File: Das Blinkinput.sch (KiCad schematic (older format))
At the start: 11 parts, among them P101 CONN_01X02, P102 CONN_01X01, P103 CONN_01X01, P104 CONN_01X01, P105 CONN_01X05, U101 LP2980IM5-3.0/NOPB

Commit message: Added photodiode component to new local footprint library
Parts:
- C101, C102: footprint (none) -> Capacitors_SMD:C_0805_HandSoldering
- P101: footprint (none) -> Pin_Headers:Pin_Header_Straight_1x02
- P102, P103, P104: footprint (none) -> Pin_Headers:Pin_Header_Straight_1x01
- P105: footprint (none) -> Pin_Headers:Pin_Header_Straight_1x05
- R101, R102, R103: footprint (none) -> Resistors_SMD:R_0805_HandSoldering
- U101: footprint (none) -> Housings_SOT-23_SOT-143_TSOT-6:SOT-23-5
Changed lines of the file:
@@
 F 0 "P105" H 8250 1900 50  0000 C CNN
 F 1 "CONN_01X05" V 8350 1600 50  0000 C CNN
-F 2 "" H 8250 1600 60  0000 C CNN
+F 2 "Pin_Headers:Pin_Header_Straight_1x05" H 8250 1600 60  0001 C CNN
 F 3 "" H 8250 1600 60  0000 C CNN
 	1    8250 1600
@@
 F 0 "P101" H 750 1800 50  0000 C CNN
 F 1 "CONN_01X02" V 850 1650 50  0000 C CNN
-F 2 "" H 750 1650 60  0000 C CNN
+F 2 "Pin_Headers:Pin_Header_Straight_1x02" H 750 1650 60  0001 C CNN
 F 3 "" H 750 1650 60  0000 C CNN
 	1    750  1650
@@
 F 0 "U101" H 2900 1450 60  0000 C CNN
 F 1 "LP2980IM5-3.0/NOPB" H 2700 2350 60  0000 C CNN
-F 2 "" H 2700 1900 60  0000 C CNN
+F 2 "Housings_SOT-23_SOT-143_TSOT-6:SOT-23-5" H 2700 1900 60  0001 C CNN
 F 3 "" H 2700 1900 60  0000 C CNN
 	1    2700 1900
@@
 F 0 "C101" H 1375 2050 50  0000 L CNN
 F 1 "1U" H 1375 1850 50  0000 L CNN
-F 2 "" H 1388 1800 30  0000 C CNN
+F 2 "Capacitors_SMD:C_0805_HandSoldering" H 1388 1800 30  0001 C CNN
 F 3 "" H 1350 1950 60  0000 C CNN
 	1    1350 1950
@@
 F 0 "C102" H 3725 2150 50  0000 L CNN
 F 1 "1U" H 3725 1950 50  0000 L CNN
-F 2 "" H 3738 1900 30  0000 C CNN
+F 2 "Capacitors_SMD:C_0805_HandSoldering" H 3738 1900 30  0001 C CNN
 F 3 "" H 3700 2050 60  0000 C CNN
 	1    3700 2050
@@
 F 0 "R101" V 1730 2300 50  0000 C CNN
 F 1 "0" V 1650 2300 50  0000 C CNN
-F 2 "" V 1580 2300 30  0000 C CNN
+F 2 "Resistors_SMD:R_0805_HandSoldering" V 1580 2300 30  0001 C CNN
 F 3 "" H 1650 2300 30  0000 C CNN
 	1    1650 2300
@@
 F 0 "R102" V 2280 5150 50  0000 C CNN
 F 1 "10K" V 2200 5150 50  0000 C CNN
-F 2 "" V 2130 5150 30  0000 C CNN
+F 2 "Resistors_SMD:R_0805_HandSoldering" V 2130 5150 30  0001 C CNN
 F 3 "" H 2200 5150 30  0000 C CNN
 	1    2200 5150
@@
 F 0 "R103" V 2280 5700 50  0000 C CNN
 F 1 "10K" V 2200 5700 50  0000 C CNN
-F 2 "" V 2130 5700 30  0000 C CNN
+F 2 "Resistors_SMD:R_0805_HandSoldering" V 2130 5700 30  0001 C CNN
 F 3 "" H 2200 5700 30  0000 C CNN
 	1    2200 5700
@@
 F 0 "P103" H 3600 1150 50  0000 C CNN
 F 1 "CONN_01X01" V 3700 1050 50  0000 C CNN
-F 2 "" H 3600 1050 60  0000 C CNN
+F 2 "Pin_Headers:Pin_Header_Straight_1x01" H 3600 1050 60  0001 C CNN
 F 3 "" H 3600 1050 60  0000 C CNN
 	1    3600 1050
@@
 F 0 "P102" H 2700 4950 50  0000 C CNN
 F 1 "CONN_01X01" V 2800 4850 50  0000 C CNN
-F 2 "" H 2700 4850 60  0000 C CNN
+F 2 "Pin_Headers:Pin_Header_Straight_1x01" H 2700 4850 60  0001 C CNN
 F 3 "" H 2700 4850 60  0000 C CNN
 	1    2700 4850
@@
 F 0 "P104" H 3650 3250 50  0000 C CNN
 F 1 "CONN_01X01" V 3750 3150 50  0000 C CNN
-F 2 "" H 3650 3150 60  0000 C CNN
+F 2 "Pin_Headers:Pin_Header_Straight_1x01" H 3650 3150 60  0001 C CNN
 F 3 "" H 3650 3150 60  0000 C CNN
 	1    3650 3150

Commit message: Routed remainder of lines and added test points with lables
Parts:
- added P106: CONN_01X01, Pin_Headers:Pin_Header_Straight_1x01, symbol CONN_01X01
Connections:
- net Channel1Photodetect/REF_OUT: now also P106.1 (P1)
- net Channel1Photodetect/Channel1_Out renamed Channel1Photodetect/PD2
- net Channel2Photodetect/Channel2_Out renamed Channel2Photodetect/PD3
- net Channel3Photodetect/Channel3_Out renamed Channel3Photodetect/PD5
- net Channel4Photodetect/Channel4_Out renamed Channel4Photodetect/PD4
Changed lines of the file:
@@
 F0 "Channel1Photodetect" 60
 F1 "Channel1Photodetect.sch" 60
-F2 "Channel1_Out" I R 6500 1400 60
-F3 "REF_OUT" I L 5050 1700 60
+F2 "REF_OUT" I L 5050 1700 60
+F3 "PD2" I R 6500 1400 60
 $EndSheet
 $Sheet
@@
 F0 "Channel2Photodetect" 60
 F1 "Channel2Photodetect.sch" 60
-F2 "Channel2_Out" I R 6500 2950 60
-F3 "REF_IN" I L 5100 3300 60
+F2 "REF_IN" I L 5100 3300 60
+F3 "PD3" I R 6500 2950 60
 $EndSheet
 $Sheet
@@
 F0 "Channel4Photodetect" 60
 F1 "Channel4Photodetect.sch" 60
-F2 "Channel4_Out" I R 6500 5900 60
-F3 "REF_IN" I L 5100 6200 60
+F2 "REF_IN" I L 5100 6200 60
+F3 "PD4" I R 6500 5900 60
 $EndSheet
 $Sheet
@@
 F0 "Channel3Photodetect" 60
 F1 "Channel3Photodetect.sch" 60
-F2 "Channel3_Out" I R 6600 4400 60
-F3 "REF_IN" I L 5150 4750 60
+F2 "REF_IN" I L 5150 4750 60
+F3 "PD5" I R 6600 4400 60
 $EndSheet
 $Comp
@@
 	1    0    0    -1
 $EndComp
-Wire Wire Line
-	5050 1700 4850 1700
-Wire Wire Line
-	4850 1700 4850 6200
-Wire Wire Line
-	4850 3300 5100 3300
-Wire Wire Line
-	4850 4750 5150 4750
-Connection ~ 4850 3300
-Wire Wire Line
-	4850 6200 5100 6200
-Connection ~ 4850 4750
-Wire Wire Line
-	8050 1400 6500 1400
-Wire Wire Line
-	6500 2950 6800 2950
-Wire Wire Line
-	6800 2950 6800 1500
-Wire Wire Line
-	6800 1500 8050 1500
-Wire Wire Line
-	6600 4400 7000 4400
-Wire Wire Line
-	7000 4400 7000 1600
-Wire Wire Line
-	7000 1600 8050 1600
-Wire Wire Line
-	6500 5900 7200 5900
-Wire Wire Line
-	7200 5900 7200 1700
-Wire Wire Line
-	7200 1700 8050 1700
-Wire Wire Line
-	8050 1800 7850 1800
-Wire Wire Line
-	7850 1800 7850 2450
-Wire Wire Line
-	1100 1900 1100 1700
-Wire Wire Line
-	1100 1700 950  1700
-Wire Wire Line
-	950  1600 1900 1600
-Wire Wire Line
-	1350 1600 1350 1800
-Connection ~ 1350 1600
-Wire Wire Line
-	1350 2100 1350 2800
-Wire Wire Line
-	1350 2800 3700 2800
-Wire Wire Line
-	2700 2800 2700 2600
-Wire Wire Line
-	3700 2800 3700 2200
-Connection ~ 2700 2800
-Wire Wire Line
-	3500 1600 4000 1600
-Wire Wire Line
-	3700 1600 3700 1900
 $Comp
 L R R101
@@
 	1    0    0    -1
 $EndComp
-Wire Wire Line
-	1650 2150 1650 1800
-Wire Wire Line
-	1650 1800 1900 1800
-Wire Wire Line
-	1650 2450 1650 2800
-Connection ~ 1650 2800
-Connection ~ 3700 1600
 Text GLabel 4000 1600 2    60   Input ~ 0
 3V
@@
 Text GLabel 1900 4700 0    60   Input ~ 0
 3V
-Wire Wire Line
-	1900 4700 2200 4700
-Wire Wire Line
-	2200 4700 2200 5000
-Wire Wire Line
-	2200 5300 2200 5550
-Wire Wire Line
-	2200 5850 2200 6300
 $Comp
 L GND #PWR03
@@
 	1    0    0    -1
 $EndComp
-Wire Wire Line
-	2450 2850 2450 2800
-Connection ~ 2450 2800
 $Comp
 L GND #PWR04
@@
 	1    0    0    -1
 $EndComp
-Wire Wire Line
-	2200 5400 2850 5400
-Connection ~ 2200 5400
 Text GLabel 2850 5400 2    60   Input ~ 0
 VGND
@@
 	0    -1   -1   0
 $EndComp
-Wire Wire Line
-	3600 1250 3600 1600
-Connection ~ 3600 1600
 $Comp
 L CONN_01X01 P102
@@
 	0    -1   -1   0
 $EndComp
-Wire Wire Line
-	2700 5050 2700 5400
-Connection ~ 2700 5400
 $Comp
 L CONN_01X01 P104
@@
 	0    1    1    0
 $EndComp
+Connection ~ 3650 2800
 Wire Wire Line
 	3650 2950 3650 2800
-Connection ~ 3650 2800
+Connection ~ 2700 5400
+Wire Wire Line
+	2700 5050 2700 5400
+Connection ~ 3600 1600
+Wire Wire Line
+	3600 1250 3600 1600
+Connection ~ 2200 5400
+Wire Wire Line
+	2200 5400 2850 5400
+Connection ~ 2450 2800
+Wire Wire Line
+	2450 2850 2450 2800
+Wire Wire Line
+	2200 5850 2200 6300
+Wire Wire Line
+	2200 5300 2200 5550
+Wire Wire Line
+	2200 4700 2200 5000
+Wire Wire Line
+	1900 4700 2200 4700
+Connection ~ 3700 1600
+Connection ~ 1650 2800
+Wire Wire Line
+	1650 2450 1650 2800
+Wire Wire Line
+	1650 1800 1900 1800
+Wire Wire Line
+	1650 2150 1650 1800
+Wire Wire Line
+	3700 1600 3700 1900
+Wire Wire Line
+	3500 1600 4000 1600
+Connection ~ 2700 2800
+Wire Wire Line
+	3700 2800 3700 2200
+Wire Wire Line
+	2700 2800 2700 2600
+Wire Wire Line
+	1350 2800 3700 2800
+Wire Wire Line
+	1350 2100 1350 2800
+Connection ~ 1350 1600
+Wire Wire Line
+	1350 1600 1350 1800
+Wire Wire Line
+	950  1600 1900 1600
+Wire Wire Line
+	1100 1700 950  1700
+Wire Wire Line
+	1100 1900 1100 1700
+Wire Wire Line
+	7850 1800 7850 2450
+Wire Wire Line
+	8050 1800 7850 1800
+Wire Wire Line
+	7200 1700 8050 1700
+Wire Wire Line
+	7200 5900 7200 1700
+Wire Wire Line
+	6500 5900 7200 5900
+Wire Wire Line
+	7000 1600 8050 1600
+Wire Wire Line
+	7000 4400 7000 1600
+Wire Wire Line
+	6600 4400 7000 4400
+Wire Wire Line
+	6800 1500 8050 1500
+Wire Wire Line
+	6800 2950 6800 1500
+Wire Wire Line
+	6500 2950 6800 2950
+Wire Wire Line
+	8050 1400 6500 1400
+Connection ~ 4850 4750
+Wire Wire Line
+	4850 6200 5100 6200
+Connection ~ 4850 3300
+Wire Wire Line
+	4850 4750 5150 4750
+Wire Wire Line
+	4850 3300 5100 3300
+Wire Wire Line
+	4850 1700 4850 6200
+Wire Wire Line
+	5050 1700 4850 1700
+$Comp
+L CONN_01X01 P106
+U 1 1 5560D7BE
+P 4450 4400
+F 0 "P106" H 4450 4500 50  0000 C CNN
+F 1 "CONN_01X01" V 4550 4400 50  0000 C CNN
+F 2 "Pin_Headers:Pin_Header_Straight_1x01" H 4450 4400 60  0001 C CNN
+F 3 "" H 4450 4400 60  0000 C CNN
+	1    4450 4400
+	-1   0    0    1
+$EndComp
+Wire Wire Line
+	4650 4400 4850 4400
+Connection ~ 4850 4400
 $EndSCHEMATC

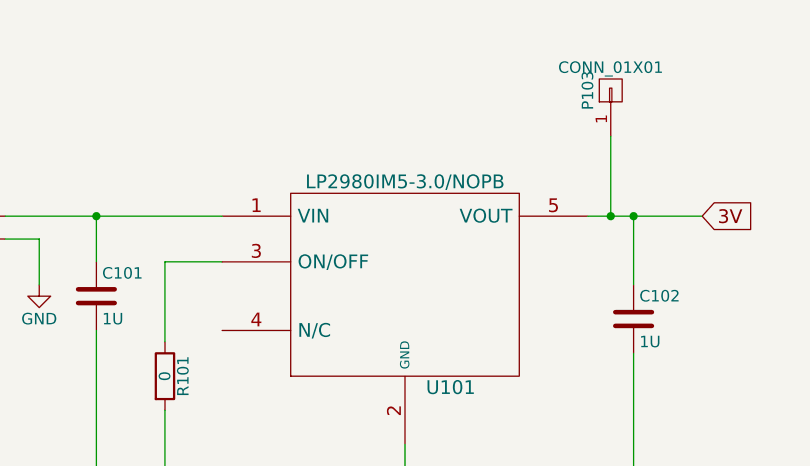
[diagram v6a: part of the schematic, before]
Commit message: Changed linear regulator to list full part number in MPN field.
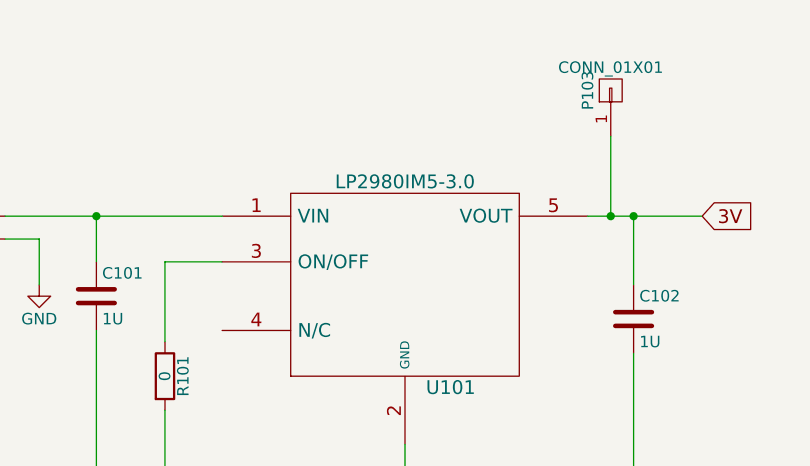
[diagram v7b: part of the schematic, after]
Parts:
- U101: value LP2980IM5-3.0/NOPB -> LP2980IM5-3.0; Link (none) -> http://parts.io/detail/12193012/LP2980IM5-3.0%2FNOPB; MPN (none) -> LP2980IM5-3.0/NOPB
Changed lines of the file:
@@
 P 2700 1900
 F 0 "U101" H 2900 1450 60  0000 C CNN
-F 1 "LP2980IM5-3.0/NOPB" H 2700 2350 60  0000 C CNN
+F 1 "LP2980IM5-3.0" H 2700 2350 60  0000 C CNN
 F 2 "Housings_SOT-23_SOT-143_TSOT-6:SOT-23-5" H 2700 1900 60  0001 C CNN
 F 3 "" H 2700 1900 60  0000 C CNN
+F 4 "LP2980IM5-3.0/NOPB" H 2700 1900 60  0001 C CNN "MPN"
+F 5 "http://parts.io/detail/12193012/LP2980IM5-3.0%2FNOPB" H 2700 1900 60  0001 C CNN "Link"
 	1    2700 1900
 	1    0    0    -1
